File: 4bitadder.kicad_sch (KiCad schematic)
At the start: 28 parts, among them SW1 1A, SW10 MASTER_SW, SW11 VOLTS_SW, SW2 2A, SW3 4A, SW4 8A, SW5 1B, SW6 2B, SW7 4B, SW8 8B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

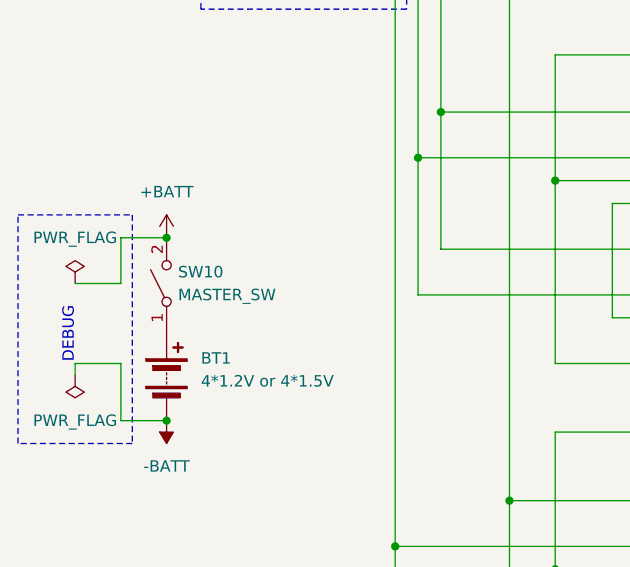
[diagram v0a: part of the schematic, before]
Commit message: Change switch design. Unroute all vias.
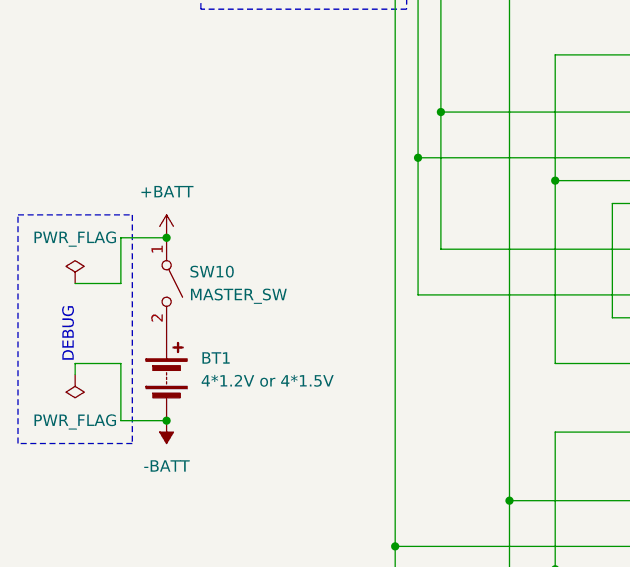
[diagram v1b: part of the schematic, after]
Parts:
- BT1: footprint _4bitadder:PAD_Battery Terminal -> 4bitadder:PAD_Battery Terminal
- D1, D2, D3, D4, D5: footprint _4bitadder:LED_WP710A10SURDK5V -> 4bitadder:LED_WP710A10SURDK5V
- SW1, SW10, SW2, SW3, SW4, SW5, SW6, SW7, SW8, SW9: footprint _4bitadder:SW_GF-123-0054 -> 4bitadder:SW-R2-1A-F-1-0
- SW11: footprint _4bitadder:SW_SLW-121586-5A-D -> 4bitadder:SW_SLW-121586-5A-D
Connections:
- net +BATT: now also SW10.1 (A); no longer SW10.2 (B)
- net at BT1.1 (+): now also SW10.2 (B); no longer SW10.1 (A)
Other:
- moved on the sheet: SW10
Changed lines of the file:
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@@
   (junction (at 215.9 31.75) (diameter 0) (color 0 0 0 0)
   )
+  (junction (at 35.56 132.08) (diameter 0) (color 0 0 0 0)
+  )
   (junction (at 63.5 123.19) (diameter 0) (color 0 0 0 0)
   )
@@
   )
   (junction (at 76.2 52.07) (diameter 0) (color 0 0 0 0)
-  )
-  (junction (at 35.56 132.08) (diameter 0) (color 0 0 0 0)
   )
   (junction (at 78.74 125.73) (diameter 0) (color 0 0 0 0)
@@
       (effects (font (size 1.27 1.27)))
     )
-    (property "Footprint" "_4bitadder:LED_WP710A10SURDK5V" (at 168.91 36.83 0)
+    (property "Footprint" "4bitadder:LED_WP710A10SURDK5V" (at 168.91 36.83 0)
       (effects (font (size 1.27 1.27)) hide)
     )
@@
       (effects (font (size 1.27 1.27)))
     )
-    (property "Footprint" "_4bitadder:LED_WP710A10SURDK5V" (at 168.91 88.9 0)
+    (property "Footprint" "4bitadder:LED_WP710A10SURDK5V" (at 168.91 88.9 0)
       (effects (font (size 1.27 1.27)) hide)
     )
@@
       (effects (font (size 1.27 1.27)))
     )
-    (property "Footprint" "_4bitadder:SW_GF-123-0054" (at 55.88 83.82 0)
+    (property "Footprint" "4bitadder:SW-R2-1A-F-1-0" (at 55.88 83.82 0)
       (effects (font (size 1.27 1.27)) hide)
     )
@@
       (effects (font (size 1.27 1.27)))
     )
-    (property "Footprint" "_4bitadder:SW_GF-123-0054" (at 55.88 33.02 0)
+    (property "Footprint" "4bitadder:SW-R2-1A-F-1-0" (at 55.88 33.02 0)
       (effects (font (size 1.27 1.27)) hide)
     )
@@
       (effects (font (size 1.27 1.27)))
     )
-    (property "Footprint" "_4bitadder:SW_GF-123-0054" (at 55.88 104.14 0)
+    (property "Footprint" "4bitadder:SW-R2-1A-F-1-0" (at 55.88 104.14 0)
       (effects (font (size 1.27 1.27)) hide)
     )
@@
     )
   )
-  (symbol (lib_id "Switch:SW_SPST") (at 35.56 137.16 90) (unit 1)
-    (in_bom yes) (on_board yes) (dnp no) (fields_autoplaced)
-    (property "Reference" "SW10" (at 36.83 135.89 90)
-      (effects (font (size 1.27 1.27)) (justify right))
-    )
-    (property "Value" "MASTER_SW" (at 36.83 138.43 90)
-      (effects (font (size 1.27 1.27)) (justify right))
-    )
-    (property "Footprint" "_4bitadder:SW_GF-123-0054" (at 35.56 137.16 0)
+  (symbol (lib_id "Switch:SW_SPST") (at 35.56 137.16 270) (unit 1)
+    (in_bom yes) (on_board yes) (dnp no) (fields_autoplaced)
+    (property "Reference" "SW10" (at 38.1 135.89 90)
+      (effects (font (size 1.27 1.27)) (justify left))
+    )
+    (property "Value" "MASTER_SW" (at 38.1 138.43 90)
+      (effects (font (size 1.27 1.27)) (justify left))
+    )
+    (property "Footprint" "4bitadder:SW-R2-1A-F-1-0" (at 35.56 137.16 0)
       (effects (font (size 1.27 1.27)) hide)
     )
@@
       (effects (font (size 1.27 1.27)))
     )
-    (property "Footprint" "_4bitadder:LED_WP710A10SURDK5V" (at 168.91 76.2 0)
+    (property "Footprint" "4bitadder:LED_WP710A10SURDK5V" (at 168.91 76.2 0)
       (effects (font (size 1.27 1.27)) hide)
     )
@@
       (effects (font (size 1.27 1.27)))
     )
-    (property "Footprint" "_4bitadder:LED_WP710A10SURDK5V" (at 168.91 49.53 0)
+    (property "Footprint" "4bitadder:LED_WP710A10SURDK5V" (at 168.91 49.53 0)
       (effects (font (size 1.27 1.27)) hide)
     )
@@
       (effects (font (size 1.27 1.27)) (justify left))
     )
-    (property "Footprint" "_4bitadder:PAD_Battery Terminal" (at 35.56 145.796 90)
+    (property "Footprint" "4bitadder:PAD_Battery Terminal" (at 35.56 145.796 90)
       (effects (font (size 1.27 1.27)) hide)
     )
@@
       (effects (font (size 1.27 1.27)))
     )
-    (property "Footprint" "_4bitadder:SW_SLW-121586-5A-D" (at 182.88 88.9 0)
+    (property "Footprint" "4bitadder:SW_SLW-121586-5A-D" (at 182.88 88.9 0)
       (effects (font (size 1.27 1.27)) hide)
     )
@@
       (effects (font (size 1.27 1.27)))
     )
-    (property "Footprint" "_4bitadder:SW_GF-123-0054" (at 55.88 22.86 0)
+    (property "Footprint" "4bitadder:SW-R2-1A-F-1-0" (at 55.88 22.86 0)
       (effects (font (size 1.27 1.27)) hide)
     )
@@
       (effects (font (size 1.27 1.27)))
     )
-    (property "Footprint" "_4bitadder:SW_GF-123-0054" (at 55.88 63.5 0)
+    (property "Footprint" "4bitadder:SW-R2-1A-F-1-0" (at 55.88 63.5 0)
       (effects (font (size 1.27 1.27)) hide)
     )
@@
       (effects (font (size 1.27 1.27)))
     )
-    (property "Footprint" "_4bitadder:SW_GF-123-0054" (at 55.88 43.18 0)
+    (property "Footprint" "4bitadder:SW-R2-1A-F-1-0" (at 55.88 43.18 0)
       (effects (font (size 1.27 1.27)) hide)
     )
@@
       (effects (font (size 1.27 1.27)))
     )
-    (property "Footprint" "_4bitadder:LED_WP710A10SURDK5V" (at 168.91 63.5 0)
+    (property "Footprint" "4bitadder:LED_WP710A10SURDK5V" (at 168.91 63.5 0)
       (effects (font (size 1.27 1.27)) hide)
     )
@@
       (effects (font (size 1.27 1.27)))
     )
-    (property "Footprint" "_4bitadder:SW_GF-123-0054" (at 55.88 93.98 0)
+    (property "Footprint" "4bitadder:SW-R2-1A-F-1-0" (at 55.88 93.98 0)
       (effects (font (size 1.27 1.27)) hide)
     )
@@
       (effects (font (size 1.27 1.27)))
     )
-    (property "Footprint" "_4bitadder:SW_GF-123-0054" (at 55.88 53.34 0)
+    (property "Footprint" "4bitadder:SW-R2-1A-F-1-0" (at 55.88 53.34 0)
       (effects (font (size 1.27 1.27)) hide)
     )
@@
       (effects (font (size 1.27 1.27)))
     )
-    (property "Footprint" "_4bitadder:SW_GF-123-0054" (at 55.88 73.66 0)
-      (effects (font (size 1.27 1.27)) hide)
-    )
+    (property "Footprint" "4bitadder:SW-R2-1A-F-1-0" (at 55.88 73.66 0)
+      (effects (font (size 1.27 1.27)) hide)
+    )
